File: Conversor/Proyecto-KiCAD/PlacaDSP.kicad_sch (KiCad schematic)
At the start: 0 parts

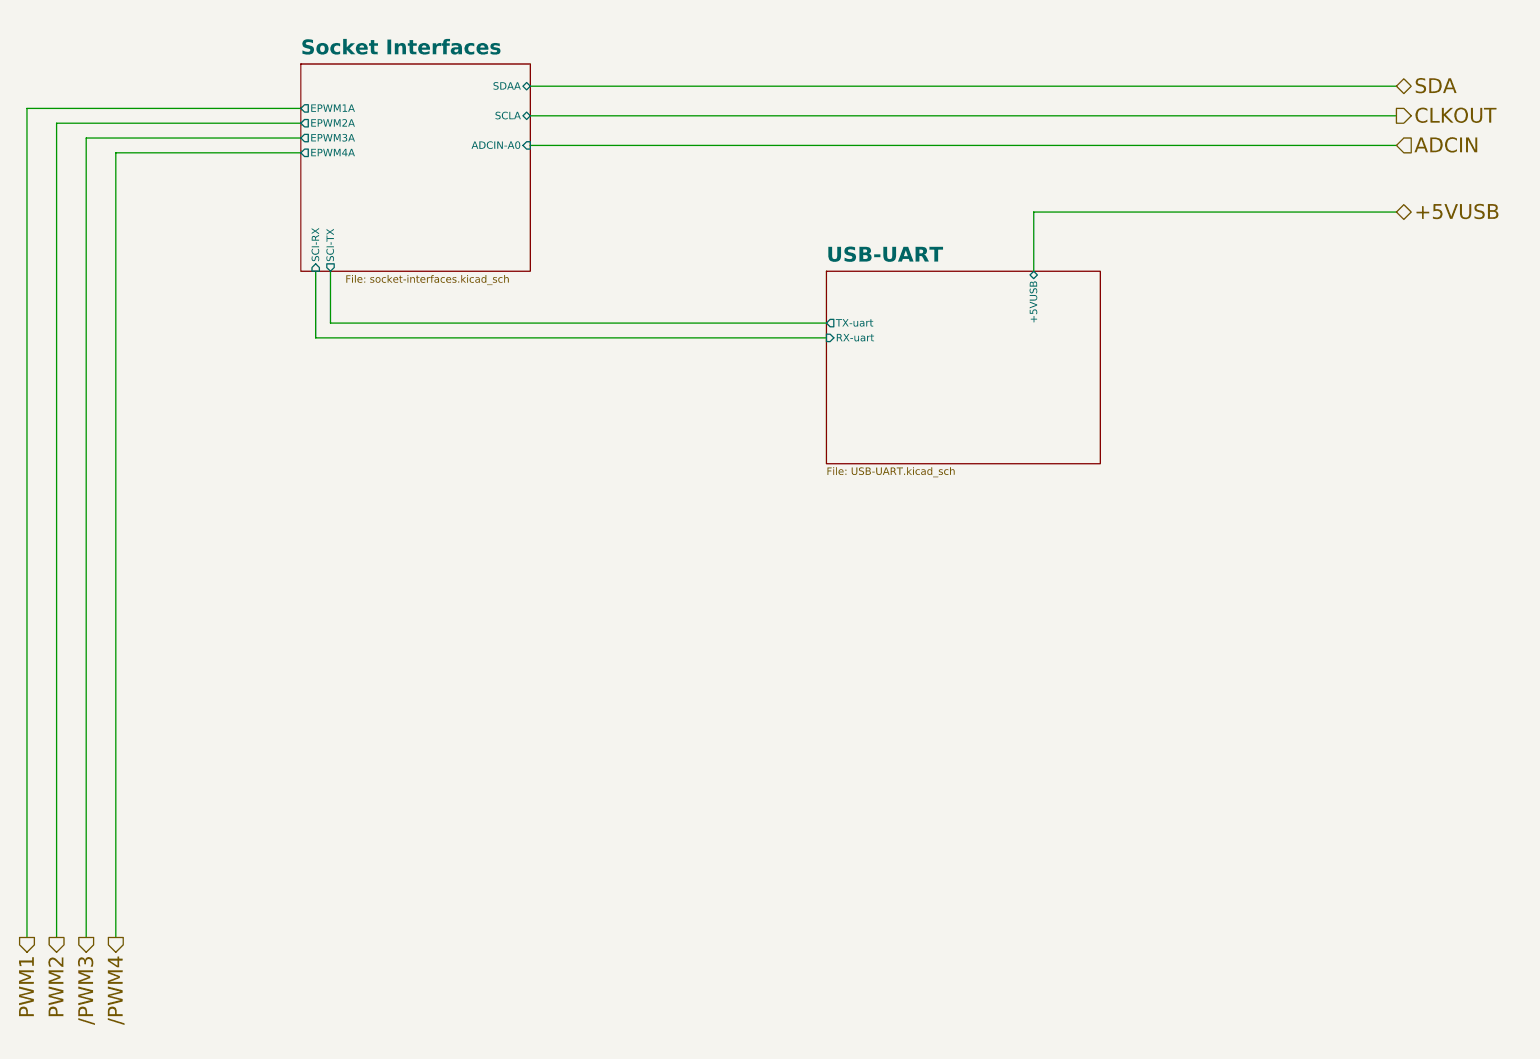
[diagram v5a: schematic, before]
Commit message: Comenzar a asignar footprints a todos los componentes
- Agregado un header para conectar el módulo de tarjeta SD de Arduino
por SPI
- Los GNDs conectados por resistencias nulas son para conectar los GNDs
en caso de que fuera necesario
- Agregar una nota de aplicaión de aislación para I2C (creo que como
estan conectados SDAO y SDAI está bien)
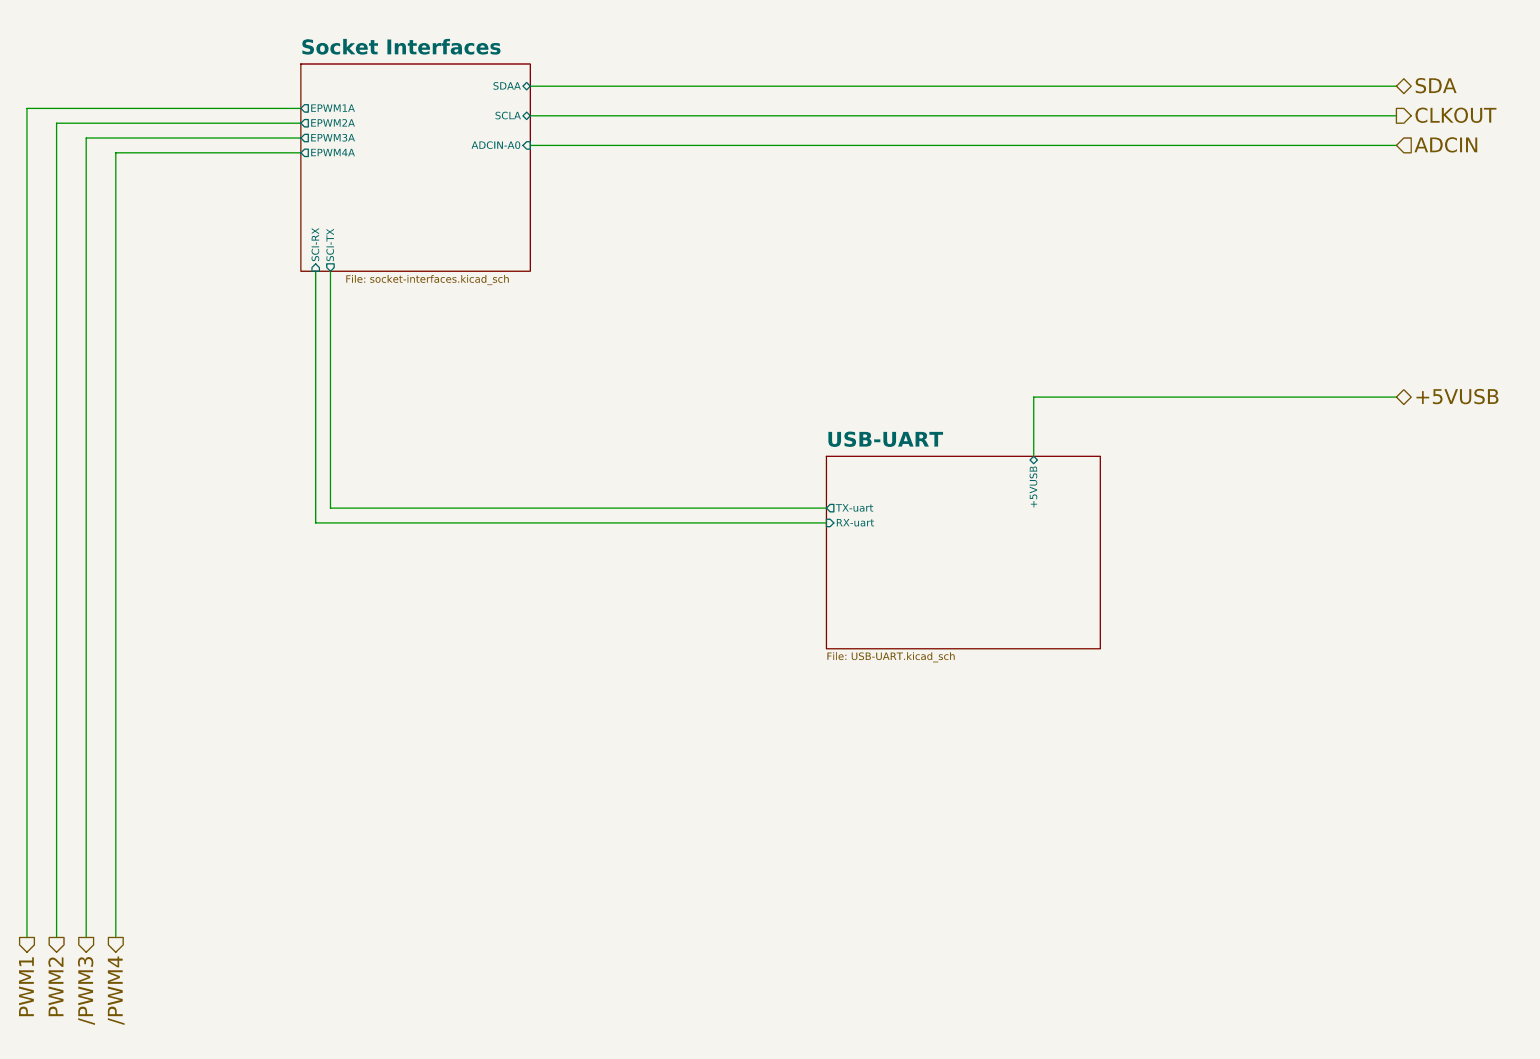
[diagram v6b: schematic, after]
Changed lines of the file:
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@@
     (stroke (width 0) (type default) (color 0 0 0 0))
   )
-  (wire (pts (xy 74.93 71.12) (xy 74.93 59.69))
+  (wire (pts (xy 74.93 102.87) (xy 74.93 59.69))
     (stroke (width 0) (type default) (color 0 0 0 0))
   )
-  (wire (pts (xy 74.93 71.12) (xy 162.56 71.12))
+  (wire (pts (xy 74.93 102.87) (xy 162.56 102.87))
     (stroke (width 0) (type default) (color 0 0 0 0))
   )
-  (wire (pts (xy 198.12 49.53) (xy 260.35 49.53))
+  (wire (pts (xy 198.12 81.28) (xy 260.35 81.28))
     (stroke (width 0) (type default) (color 0 0 0 0))
   )
@@
     (stroke (width 0) (type default) (color 0 0 0 0))
   )
-  (wire (pts (xy 77.47 68.58) (xy 77.47 59.69))
+  (wire (pts (xy 77.47 100.33) (xy 77.47 59.69))
     (stroke (width 0) (type default) (color 0 0 0 0))
   )
@@
     (stroke (width 0) (type default) (color 0 0 0 0))
   )
-  (wire (pts (xy 77.47 68.58) (xy 162.56 68.58))
+  (wire (pts (xy 77.47 100.33) (xy 162.56 100.33))
     (stroke (width 0) (type default) (color 0 0 0 0))
   )
@@
     (stroke (width 0) (type default) (color 0 0 0 0))
   )
-  (wire (pts (xy 198.12 49.53) (xy 198.12 59.69))
+  (wire (pts (xy 198.12 81.28) (xy 198.12 91.44))
     (stroke (width 0) (type default) (color 0 0 0 0))
   )
@@
     (effects (font (size 2.54 2.54)) (justify right))
   )
-  (hierarchical_label "+5VUSB" (shape bidirectional) (at 260.35 49.53 0)
+  (hierarchical_label "+5VUSB" (shape bidirectional) (at 260.35 81.28 0)
     (effects (font (size 2.54 2.54)) (justify left))
   )
-  (sheet (at 162.56 59.69) (size 46.99 33.02) (fields_autoplaced)
+  (sheet (at 162.56 91.44) (size 46.99 33.02) (fields_autoplaced)
     (stroke (width 0.1524) (type solid) (color 0 0 0 0))
     (fill (color 0 0 0 0.0000))
-    (property "Sheet name" "USB-UART" (id 0) (at 162.56 58.3434 0)
+    (property "Sheet name" "USB-UART" (id 0) (at 162.56 90.0934 0)
       (effects (font (size 2.54 2.54) bold) (justify left bottom))
     )
-    (property "Sheet file" "USB-UART.kicad_sch" (id 1) (at 162.56 93.2946 0)
+    (property "Sheet file" "USB-UART.kicad_sch" (id 1) (at 162.56 125.0446 0)
       (effects (font (size 1.27 1.27)) (justify left top))
     )
-    (pin "TX-uart" output (at 162.56 68.58 180)
+    (pin "TX-uart" output (at 162.56 100.33 180)
       (effects (font (size 1.27 1.27)) (justify left))
     )
-    (pin "RX-uart" input (at 162.56 71.12 180)
+    (pin "RX-uart" input (at 162.56 102.87 180)
       (effects (font (size 1.27 1.27)) (justify left))
     )
-    (pin "+5VUSB" bidirectional (at 198.12 59.69 90)
+    (pin "+5VUSB" bidirectional (at 198.12 91.44 90)
       (effects (font (size 1.27 1.27)) (justify right))
     )
